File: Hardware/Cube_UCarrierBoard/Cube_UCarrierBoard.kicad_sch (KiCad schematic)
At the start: 1 part

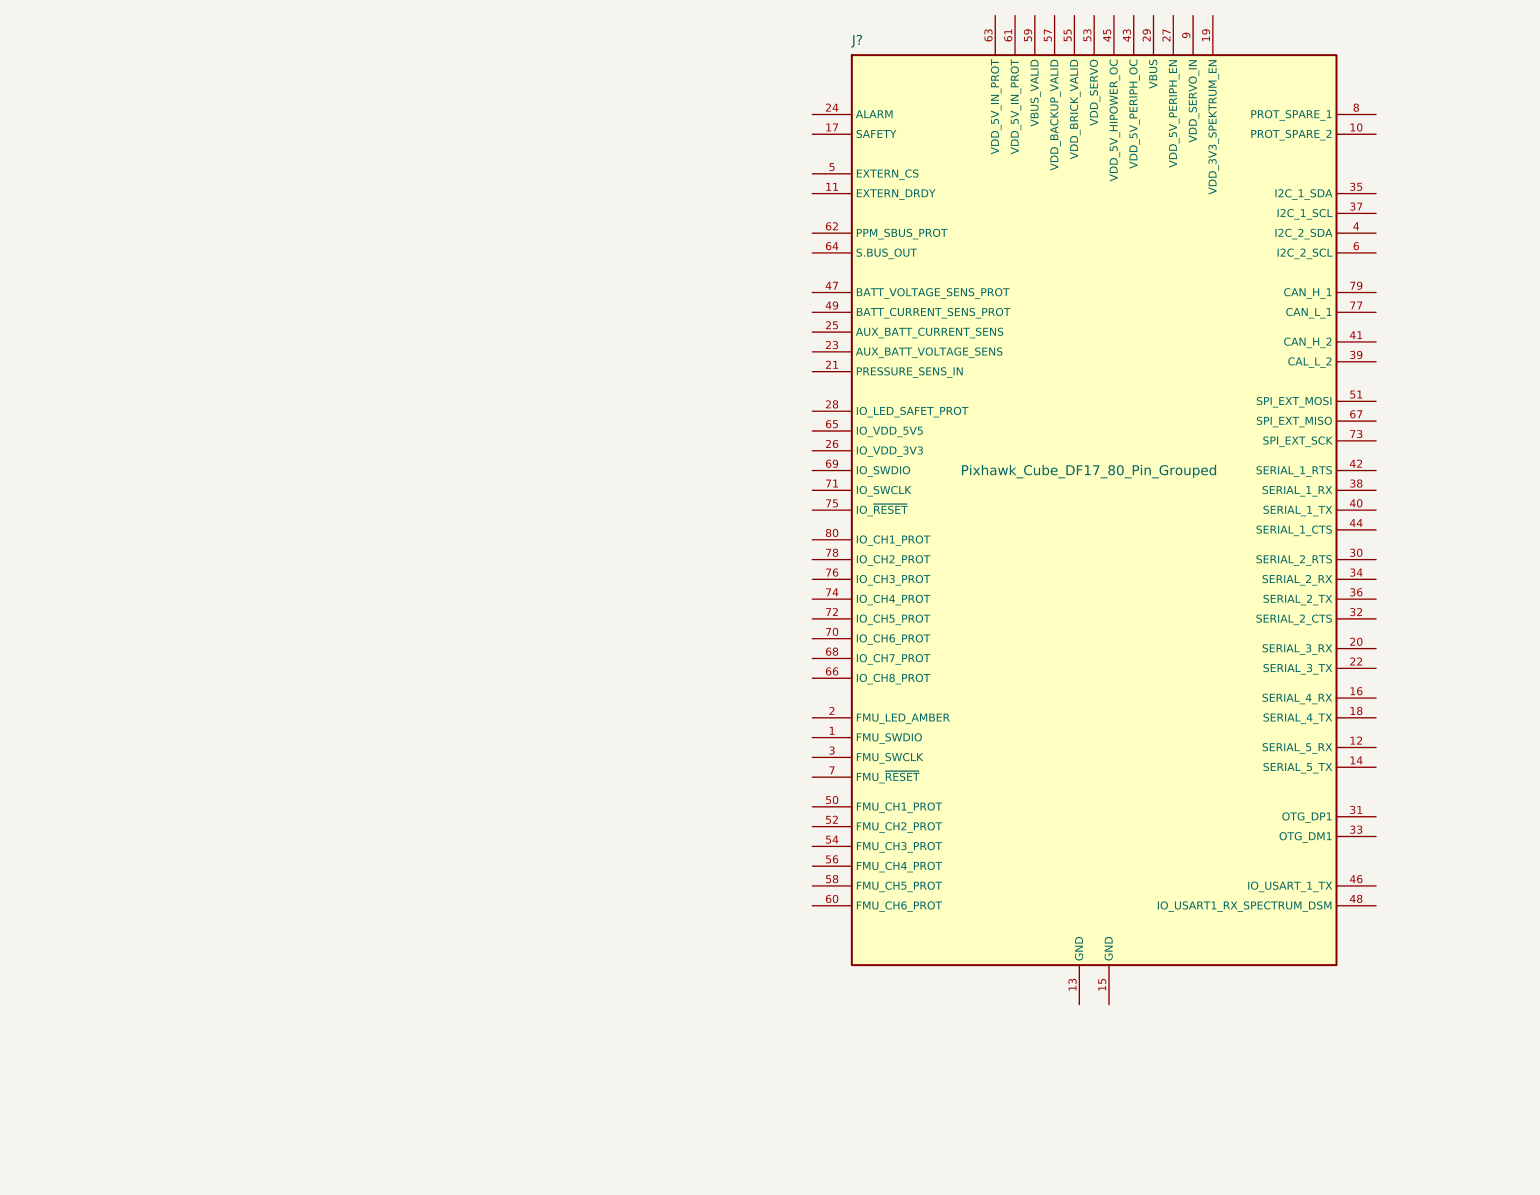
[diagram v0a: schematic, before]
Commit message: Added servo and power connectors
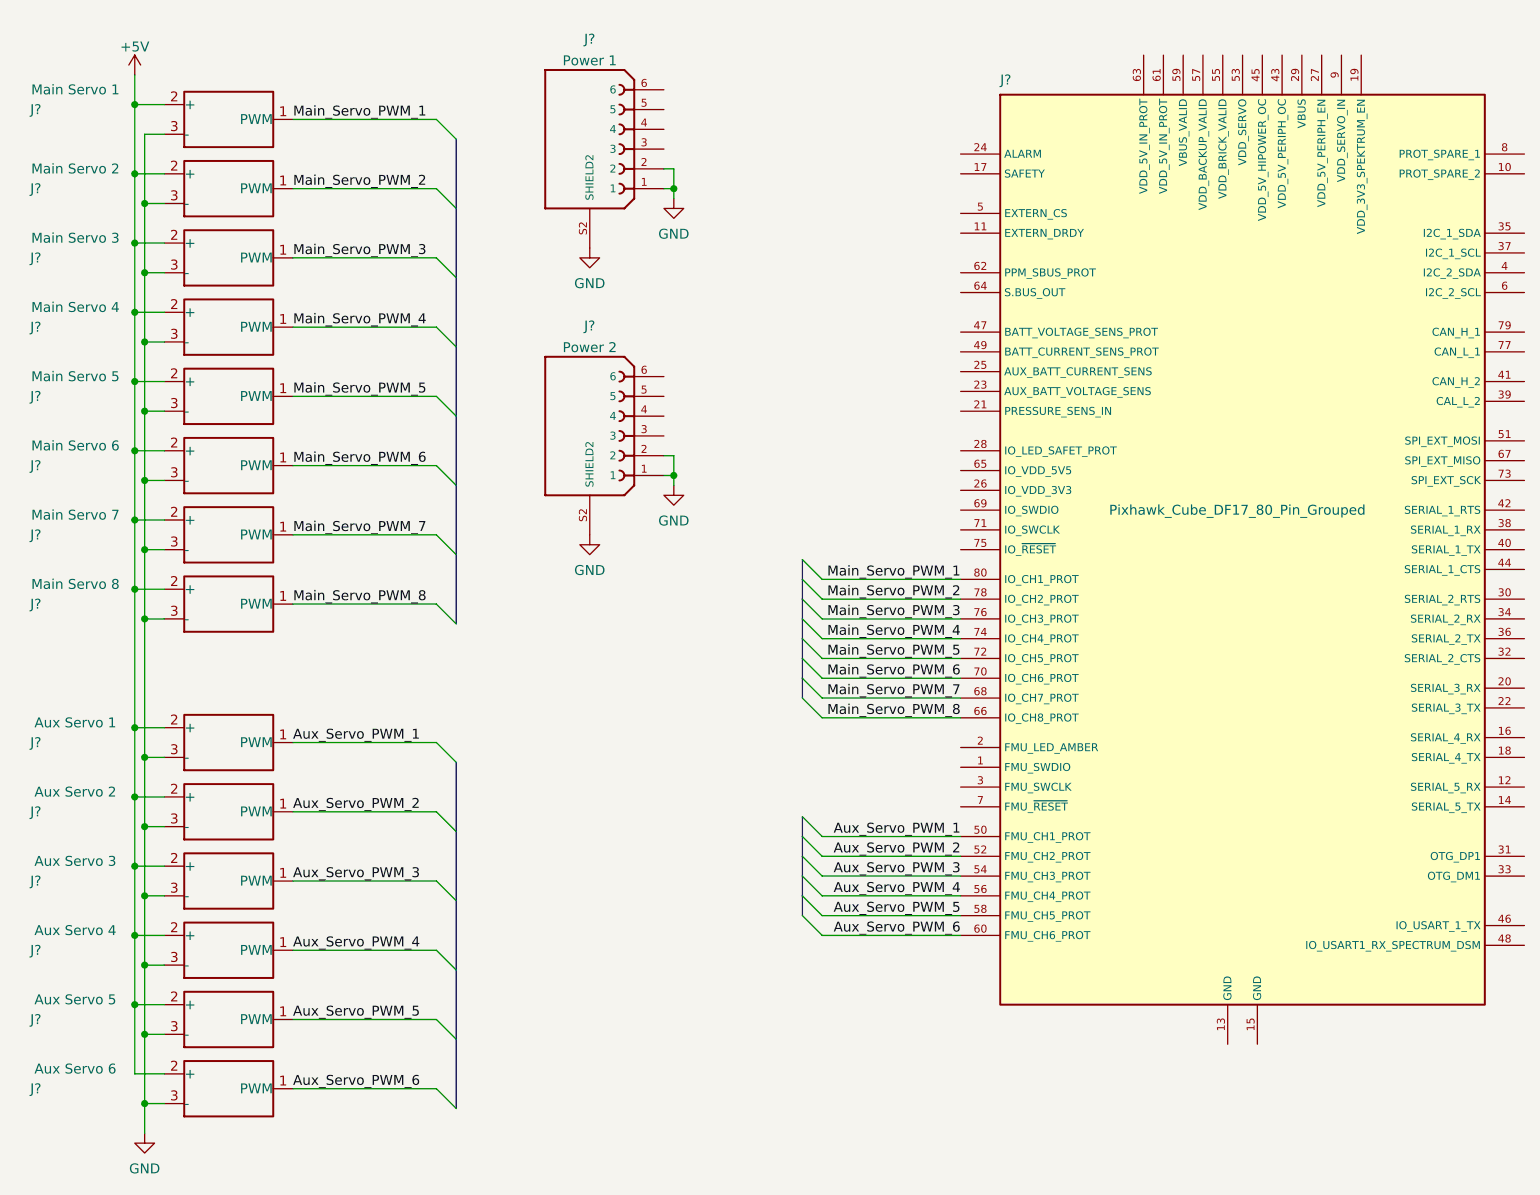
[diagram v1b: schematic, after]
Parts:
- added J?: Main Servo 7, symbol CubeCarrierBoard:Motor_Servo_Futaba_J
- added J?: Aux Servo 2, symbol CubeCarrierBoard:Motor_Servo_Futaba_J
- added J?: Main Servo 8, symbol CubeCarrierBoard:Motor_Servo_Futaba_J
- added J?: Aux Servo 3, symbol CubeCarrierBoard:Motor_Servo_Futaba_J
- added J?: Main Servo 6, symbol CubeCarrierBoard:Motor_Servo_Futaba_J
- added J?: Aux Servo 5, symbol CubeCarrierBoard:Motor_Servo_Futaba_J
- added J?: Main Servo 2, symbol CubeCarrierBoard:Motor_Servo_Futaba_J
- added J?: Main Servo 4, symbol CubeCarrierBoard:Motor_Servo_Futaba_J
- added J?: Power 1, MOLEX_5024430670, symbol CubeCarrierBoard:6-Pin_Clik-Mate_F
- added J?: Main Servo 1, symbol CubeCarrierBoard:Motor_Servo_Futaba_J
- added J?: Aux Servo 1, symbol CubeCarrierBoard:Motor_Servo_Futaba_J
- added J?: Main Servo 5, symbol CubeCarrierBoard:Motor_Servo_Futaba_J
- added J?: Aux Servo 4, symbol CubeCarrierBoard:Motor_Servo_Futaba_J
- added J?: Power 2, MOLEX_5024430670, symbol CubeCarrierBoard:6-Pin_Clik-Mate_F
- added J?: Main Servo 3, symbol CubeCarrierBoard:Motor_Servo_Futaba_J
- added J?: Aux Servo 6, symbol CubeCarrierBoard:Motor_Servo_Futaba_J
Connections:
- net Aux_Servo_PWM_1: now reaches J?.50 (FMU_CH1_PROT)
- net Aux_Servo_PWM_1: now also J?.1 (PWM)
- net Aux_Servo_PWM_2: now reaches J?.52 (FMU_CH2_PROT)
- net Aux_Servo_PWM_2: now also J?.1 (PWM)
- net Aux_Servo_PWM_3: now reaches J?.54 (FMU_CH3_PROT)
- net Aux_Servo_PWM_3: now also J?.1 (PWM)
- net Aux_Servo_PWM_4: now reaches J?.56 (FMU_CH4_PROT)
- net Aux_Servo_PWM_4: now also J?.1 (PWM)
- net Aux_Servo_PWM_5: now reaches J?.58 (FMU_CH5_PROT)
- net Aux_Servo_PWM_5: now also J?.1 (PWM)
- net Aux_Servo_PWM_6: now reaches J?.60 (FMU_CH6_PROT)
- net Aux_Servo_PWM_6: now also J?.1 (PWM)
- net Main_Servo_PWM_8: now reaches J?.66 (IO_CH8_PROT)
- net Main_Servo_PWM_8: now also J?.1 (PWM)
- net Main_Servo_PWM_7: now reaches J?.68 (IO_CH7_PROT)
- net Main_Servo_PWM_7: now also J?.1 (PWM)
- net Main_Servo_PWM_6: now reaches J?.70 (IO_CH6_PROT)
- net Main_Servo_PWM_6: now also J?.1 (PWM)
- net Main_Servo_PWM_5: now reaches J?.72 (IO_CH5_PROT)
- net Main_Servo_PWM_5: now also J?.1 (PWM)
- net Main_Servo_PWM_4: now reaches J?.74 (IO_CH4_PROT)
- net Main_Servo_PWM_4: now also J?.1 (PWM)
- net Main_Servo_PWM_3: now reaches J?.76 (IO_CH3_PROT)
- net Main_Servo_PWM_3: now also J?.1 (PWM)
- net Main_Servo_PWM_2: now reaches J?.78 (IO_CH2_PROT)
- net Main_Servo_PWM_2: now also J?.1 (PWM)
- net Main_Servo_PWM_1: now reaches J?.80 (IO_CH1_PROT)
- net Main_Servo_PWM_1: now also J?.1 (PWM)
- new net +5V: J?.2 (+), J?.2 (+), J?.2 (+), J?.2 (+), J?.2 (+), J?.2 (+), J?.2 (+), J?.2 (+), J?.2 (+), J?.2 (+), J?.2 (+), J?.2 (+), J?.2 (+), J?.2 (+)
- new net GND: J?.1, J?.1, J?.2, J?.2, J?.3 (-), J?.3 (-), J?.3 (-), J?.3 (-), J?.3 (-), J?.3 (-), J?.3 (-), J?.3 (-), J?.3 (-), J?.3 (-), J?.3 (-), J?.3 (-), J?.3 (-), J?.3 (-), J?.S2 (SHIELD2), J?.S2 (SHIELD2)
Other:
- moved on the sheet: J?

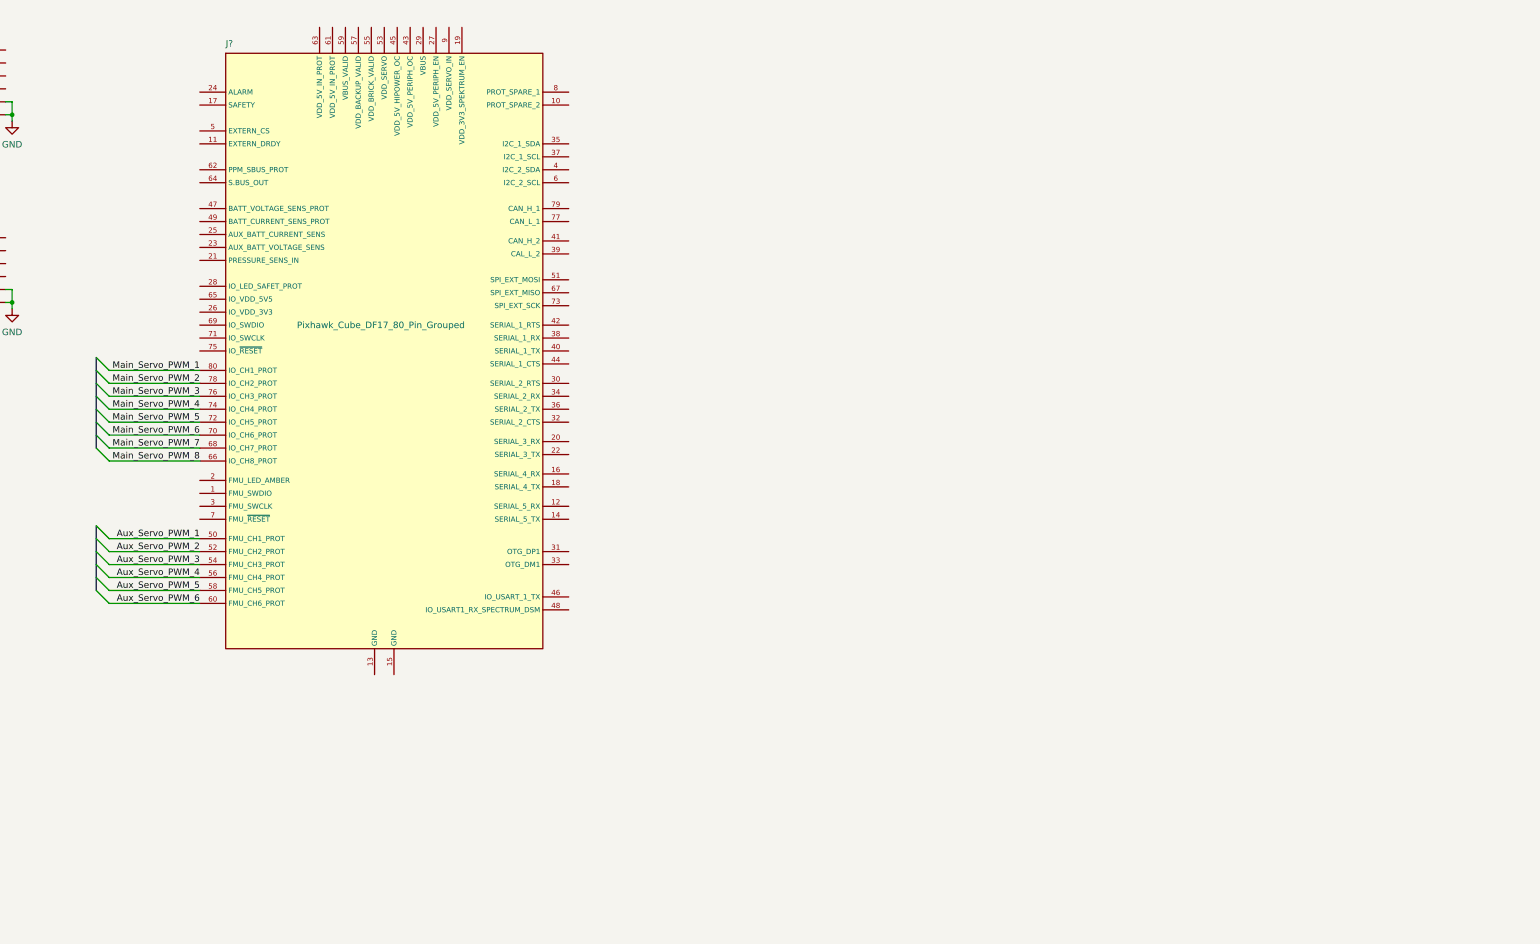
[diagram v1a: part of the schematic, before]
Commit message: Footprints & Symbols for JST & Molex connectors
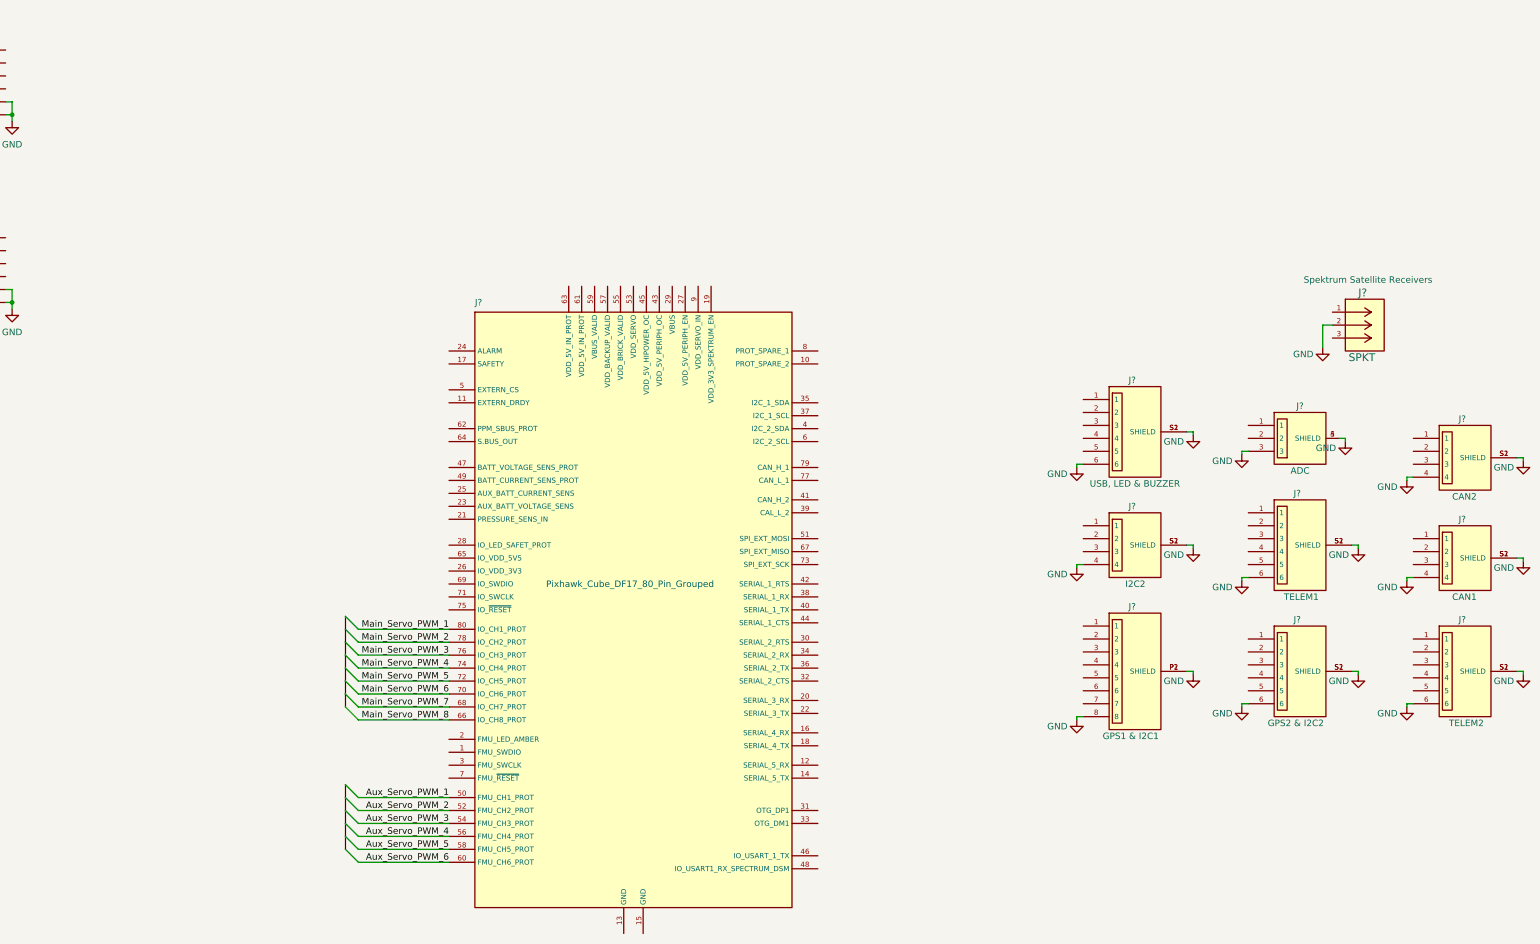
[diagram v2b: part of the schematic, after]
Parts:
- added J?: CAN1, JST_BM04B-GHS-TBT(LF)(SN)(N), symbol BM04B-GHS-TBT_LF__SN__N_:BM04B-GHS-TBT(LF)(SN)(N)
- added J?: CAN2, JST_BM04B-GHS-TBT(LF)(SN)(N), symbol BM04B-GHS-TBT_LF__SN__N_:BM04B-GHS-TBT(LF)(SN)(N)
- added J?: TELEM1, JST_BM06B-GHS-TBT(LF)(SN)(N), symbol BM06B-GHS-TBT_LF__SN__N_:BM06B-GHS-TBT(LF)(SN)(N)
- added J?: USB, LED & BUZZER, JST_BM06B-GHS-TBT(LF)(SN)(N), symbol BM06B-GHS-TBT_LF__SN__N_:BM06B-GHS-TBT(LF)(SN)(N)
- added J?: TELEM2, JST_BM06B-GHS-TBT(LF)(SN)(N), symbol BM06B-GHS-TBT_LF__SN__N_:BM06B-GHS-TBT(LF)(SN)(N)
- added J?: SPKT, CONN_S3B-ZR-SM4A-TFLFSN_JST, symbol 2022-11-05_21-49-56:S3B-ZR-SM4A-TFLFSN
- added J?: GPS1 & I2C1, JST_BM08B-GHS-TBT(LF)(SN)(N), symbol BM08B-GHS-TBT_LF__SN__N_:BM08B-GHS-TBT(LF)(SN)(N)
- added J?: ADC, CONN_BM03B-GHS-TBT(LF)(SN)(N), symbol BM03B-GHS-TBT_LF__SN__N_:BM03B-GHS-TBT(LF)(SN)(N)
- added J?: GPS2 & I2C2, JST_BM06B-GHS-TBT(LF)(SN)(N), symbol BM06B-GHS-TBT_LF__SN__N_:BM06B-GHS-TBT(LF)(SN)(N)
- added J?: I2C2, JST_BM04B-GHS-TBT(LF)(SN)(N), symbol BM04B-GHS-TBT_LF__SN__N_:BM04B-GHS-TBT(LF)(SN)(N)
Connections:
- net GND: now also J?.2, J?.3, J?.4, J?.4, J?.4, J?.4 (SHIELD), J?.5 (SHIELD), J?.6, J?.6, J?.6, J?.6, J?.8, J?.P1 (SHIELD), J?.P2 (SHIELD), J?.S1 (SHIELD), J?.S1 (SHIELD), J?.S1 (SHIELD), J?.S1 (SHIELD), J?.S1 (SHIELD), J?.S1 (SHIELD), J?.S1 (SHIELD), J?.S2 (SHIELD), J?.S2 (SHIELD), J?.S2 (SHIELD), J?.S2 (SHIELD), J?.S2 (SHIELD), J?.S2 (SHIELD), J?.S2 (SHIELD)
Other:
- moved on the sheet: J?

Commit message: Remade Power Supply Module Schematic in KiCAD
All components labeled with correct values, part numbers, footprints
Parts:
- J12, J18, J25, J26: renamed from J?; footprint JST_BM06B-GHS-TBT(LF)(SN)(N) -> libraries:JST_BM06B-GHS-TBT(LF)(SN)(N)
- J13: renamed from J?; footprint CONN_BM03B-GHS-TBT(LF)(SN)(N) -> libraries:CONN_BM03B-GHS-TBT(LF)(SN)(N)
- J14, J17, J19: renamed from J?; footprint JST_BM04B-GHS-TBT(LF)(SN)(N) -> libraries:JST_BM04B-GHS-TBT(LF)(SN)(N)
- J2, J7: renamed from J?; footprint MOLEX_5024430670 -> libraries:MOLEX_5024430670
- J21: renamed from J?; footprint (none) -> libraries:Cube_DF17_Mount
- J24: renamed from J?; footprint JST_BM08B-GHS-TBT(LF)(SN)(N) -> libraries:JST_BM08B-GHS-TBT(LF)(SN)(N)
- gave numbers to parts that had none: 15
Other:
- added sheet Power Selection Module (PSM.kicad_sch)

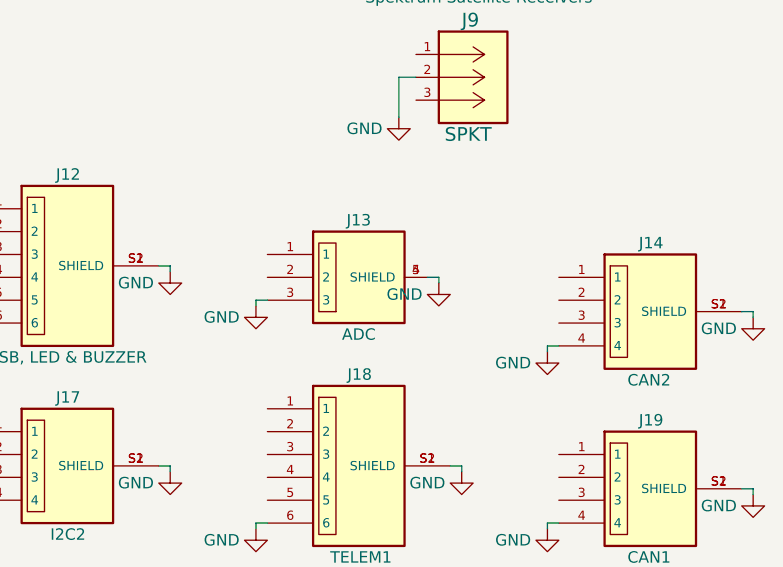
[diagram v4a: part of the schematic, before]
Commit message: Added ESC Project Files
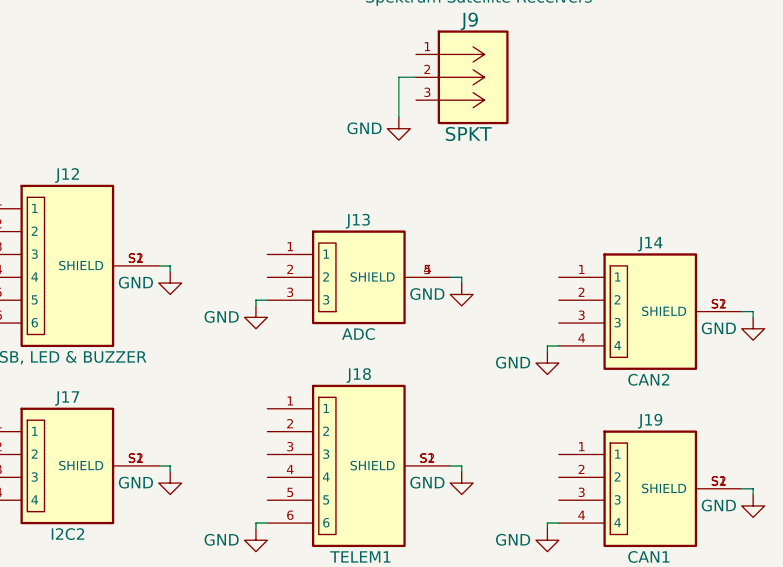
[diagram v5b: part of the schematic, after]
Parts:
- J13: footprint libraries:CONN_BM03B-GHS-TBT(LF)(SN)(N) -> CONN_BM03B-GHS-TBT(LF)(SN)(N)
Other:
- moved on the sheet: J13
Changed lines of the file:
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@@
     (stroke (width 0) (type default) (color 0 0 0 0))
   )
-  (wire (pts (xy 358.14 114.3) (xy 358.14 113.665))
+  (wire (pts (xy 360.68 114.3) (xy 360.68 113.665))
     (stroke (width 0) (type default) (color 0 0 0 0))
   )
@@
     (stroke (width 0) (type default) (color 0 0 0 0))
   )
-  (wire (pts (xy 356.87 113.665) (xy 358.14 113.665))
+  (wire (pts (xy 359.41 113.665) (xy 360.68 113.665))
     (stroke (width 0) (type default) (color 0 0 0 0))
   )
@@
     (pin "1")
   )
-  (symbol (lib_id "power:GND") (at 358.14 114.3 0) (unit 1)
-    (in_bom yes) (on_board yes)
-    (property "Reference" "#PWR08" (id 0) (at 358.14 120.65 0)
-      (effects (font (size 1.27 1.27)) hide)
-    )
-    (property "Value" "GND" (id 1) (at 354.33 115.57 0))
-    (property "Footprint" "" (id 2) (at 358.14 114.3 0)
-      (effects (font (size 1.27 1.27)) hide)
-    )
-    (property "Datasheet" "" (id 3) (at 358.14 114.3 0)
+  (symbol (lib_id "power:GND") (at 360.68 114.3 0) (unit 1)
+    (in_bom yes) (on_board yes)
+    (property "Reference" "#PWR08" (id 0) (at 360.68 120.65 0)
+      (effects (font (size 1.27 1.27)) hide)
+    )
+    (property "Value" "GND" (id 1) (at 356.87 115.57 0))
+    (property "Footprint" "" (id 2) (at 360.68 114.3 0)
+      (effects (font (size 1.27 1.27)) hide)
+    )
+    (property "Datasheet" "" (id 3) (at 360.68 114.3 0)
       (effects (font (size 1.27 1.27)) hide)
     )
@@
     (property "Reference" "J13" (id 0) (at 349.25 107.315 0))
     (property "Value" "ADC" (id 1) (at 349.25 120.015 0))
-    (property "Footprint" "libraries:CONN_BM03B-GHS-TBT(LF)(SN)(N)" (id 2) (at 347.345 116.205 0)
+    (property "Footprint" "CONN_BM03B-GHS-TBT(LF)(SN)(N)" (id 2) (at 347.345 116.205 0)
       (effects (font (size 1.27 1.27)) (justify left bottom) hide)
     )
@@
     )
     (path "/ddbad9ad-46c2-458f-b271-773454fa53b9"
-      (reference "J13") (unit 1) (value "ADC") (footprint "libraries:CONN_BM03B-GHS-TBT(LF)(SN)(N)")
+      (reference "J13") (unit 1) (value "ADC") (footprint "CONN_BM03B-GHS-TBT(LF)(SN)(N)")
     )
     (path "/2f441851-d1e3-42fd-a383-d5c10cd6f24b"
